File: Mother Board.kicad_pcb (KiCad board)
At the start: 2 copper layers, 127 x 124.5 mm, 102 parts, among them J1 Conn_01x02, J2 USB_B_Mini, J3 Conn_02x05_Odd_Even, J5 Conn_01x03, J6 Conn_01x03, SW1 SW_Push, U1 LM2595SX-3.3_NOPB, U2 LM2595SX-5.0_NOPB, U3 FT232RL, U4 STM32F407IGTx, U5 TPS2111APWR, Y1 Crystal_GND24

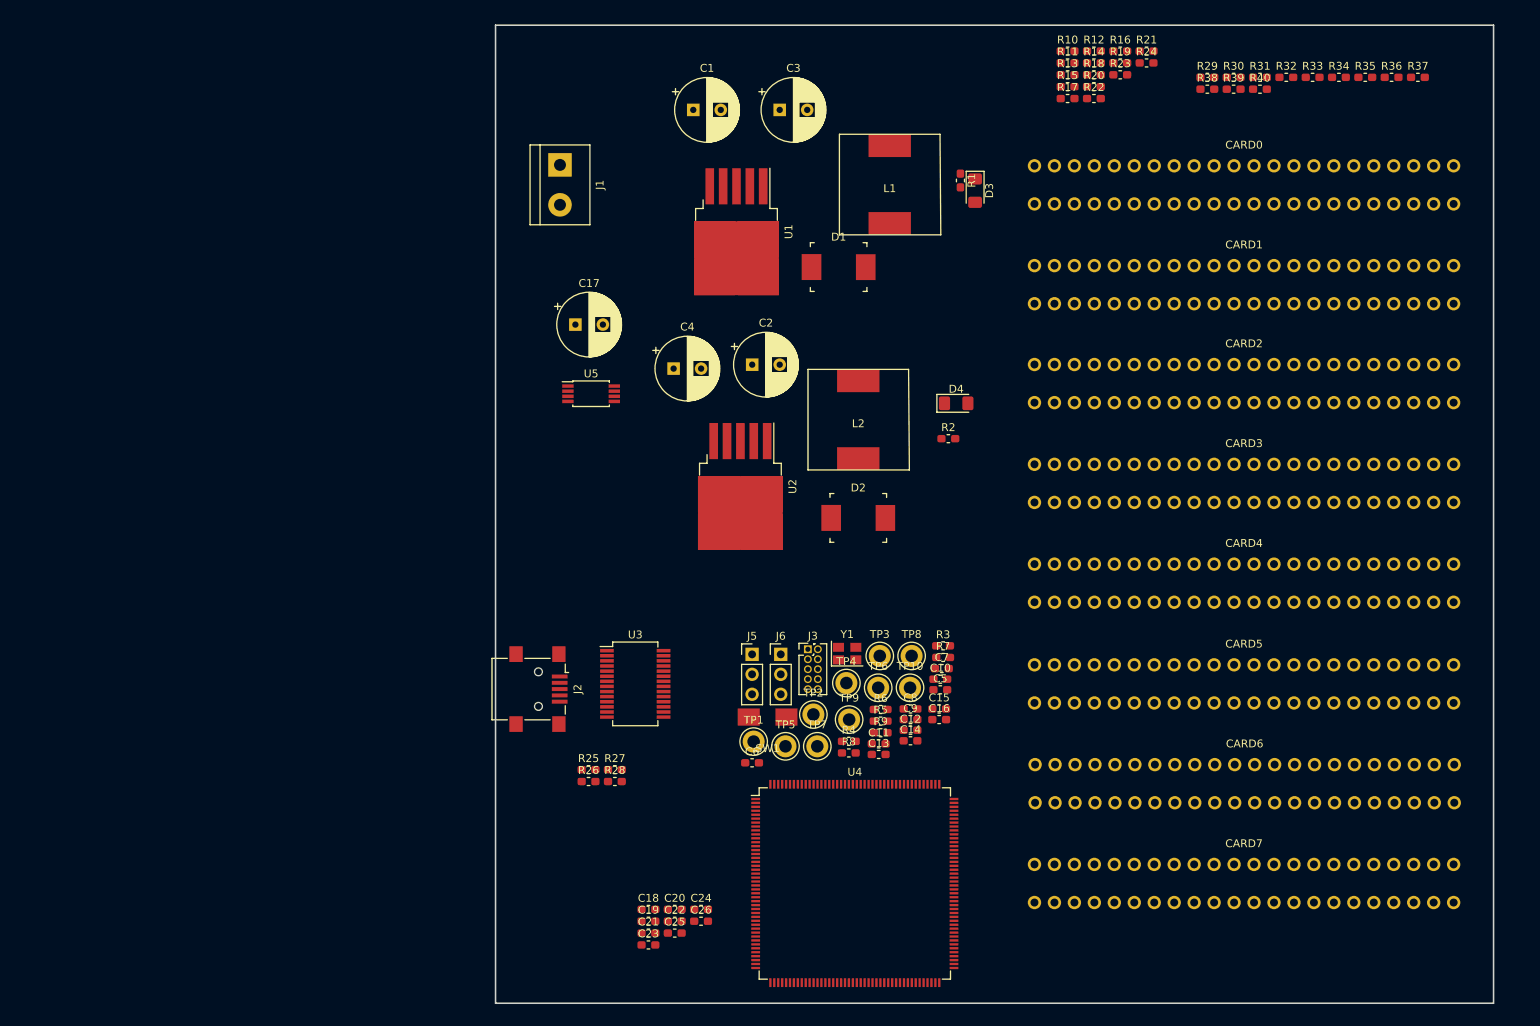
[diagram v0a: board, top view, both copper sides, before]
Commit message: Finished labeling card pins, changed rough layout
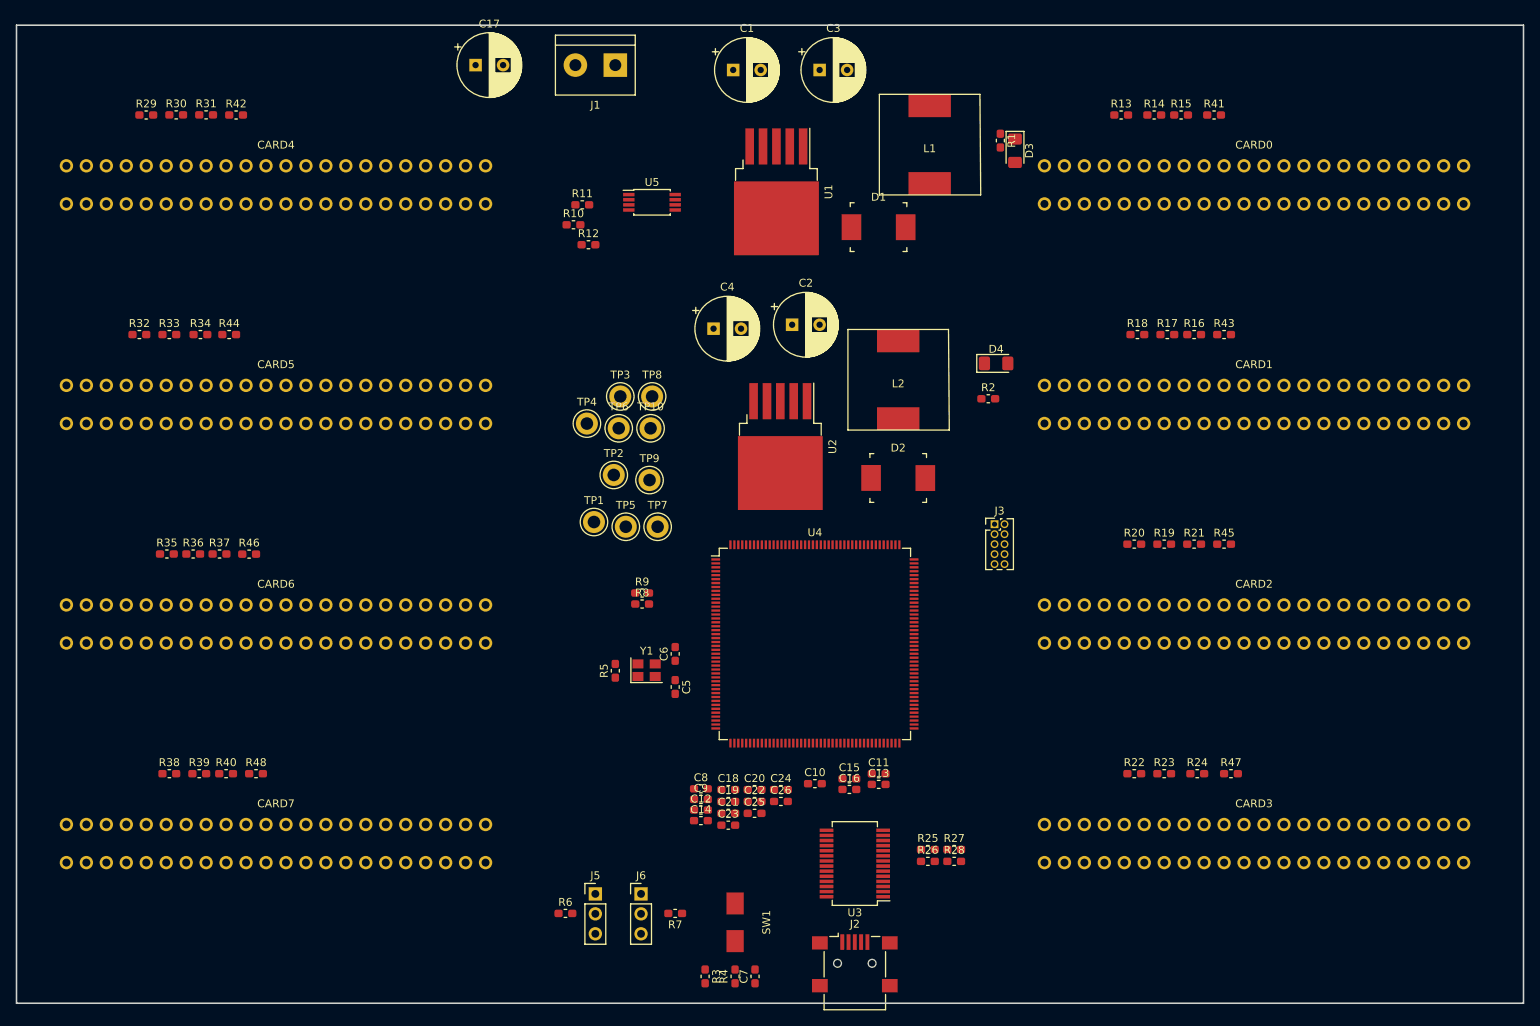
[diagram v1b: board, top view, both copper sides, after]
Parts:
- added R41: 10k, Resistor_SMD:R_0603_1608Metric_Pad1.05x0.95mm_HandSolder, F.Cu at (218.4, 47.0)
- added R42: 10k, Resistor_SMD:R_0603_1608Metric_Pad1.05x0.95mm_HandSolder, F.Cu at (94.0, 47.0)
- added R43: 10k, Resistor_SMD:R_0603_1608Metric_Pad1.05x0.95mm_HandSolder, F.Cu at (219.7, 74.9)
- added R44: 10k, Resistor_SMD:R_0603_1608Metric_Pad1.05x0.95mm_HandSolder, F.Cu at (93.1, 74.9)
- added R45: 10k, Resistor_SMD:R_0603_1608Metric_Pad1.05x0.95mm_HandSolder, F.Cu at (219.7, 101.6)
- added R46: 10k, Resistor_SMD:R_0603_1608Metric_Pad1.05x0.95mm_HandSolder, F.Cu at (95.6, 102.9)
- added R47: 10k, Resistor_SMD:R_0603_1608Metric_Pad1.05x0.95mm_HandSolder, F.Cu at (220.6, 130.8)
- added R48: 10k, Resistor_SMD:R_0603_1608Metric_Pad1.05x0.95mm_HandSolder, F.Cu at (96.5, 130.8)
- CARD0, CARD1, CARD2, CARD3, CARD4, CARD5, CARD6, CARD7: value Conn_02x22_Odd_Even -> Conn_02x22_Top_Bottom
- J1: footprint Connectors_Terminal_Blocks:TerminalBlock_bornier-2_P5.08mm -> TerminalBlock:TerminalBlock_bornier-2_P5.08mm
- U1, U2: footprint TO_SOT_Packages_SMD:TO-263-5_TabPin3 -> Package_TO_SOT_SMD:TO-263-5_TabPin3
- moved R35 164.1 mm to (85.2, 102.9)
- moved R36 164.1 mm to (88.5, 102.9)
- moved R37 164.1 mm to (91.9, 102.9)
- moved R38 158.2 mm to (85.5, 130.8)
- moved R39 157.8 mm to (89.3, 130.8)
- moved R40 157.8 mm to (92.7, 130.8)
- moved R32 149.6 mm to (81.7, 74.9)
- moved R33 149.1 mm to (85.5, 74.9)
- moved R34 148.5 mm to (89.4, 74.9)
- moved R29 135.1 mm to (82.5, 47.0)
- moved R30 134.6 mm to (86.4, 47.0)
- moved R31 134.2 mm to (90.2, 47.0)
- moved CARD4 133.2 mm to (99.1, 55.9)
- moved CARD5 128.2 mm to (99.1, 83.8)
- moved CARD6 124.9 mm to (99.1, 111.8)
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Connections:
- net CARD2_GPIO2 renamed CARD2_TIM1_CH3N
- net CARD2_GPIO4 renamed CARD2_GPIO0
- net CARD2_GPIO5 renamed CARD2_TIM10_CH1
- net CARD3_GPIO5 renamed CARD3_TIM11_CH1
- net Net-(CARD3-Pad35) renamed CARD3_TIM1_CH4
- net Net-(CARD3-Pad37) renamed CARD3_TIM3_CH4
- net Net-(CARD4-Pad35) renamed CARD4_TIM8_CH1
- net Net-(CARD4-Pad37) renamed CARD4_TIM5_CH1
- net Net-(CARD5-Pad37) renamed CARD5_TIM5_CH2
- net Net-(CARD6-Pad37) renamed CARD6_TIM5_CH3
- net Net-(CARD7-Pad37) renamed CARD7_TIM5_CH4
- CARD0 pad 10: +3V3 -> IC1_SDA
- CARD0 pad 11: +3V3 -> /CARD0_ADD0
- CARD0 pad 12: +3V3 -> /CARD0_ADD1
- CARD0 pad 13: GND -> /CARD0_ADD2
- CARD0 pad 14: GND -> CARD0_ENABLE
- CARD0 pad 15: GND -> CARD0_STATUS
- CARD0 pad 16: GND -> USART1_TX
- CARD0 pad 17: IC1_SCL -> USART1_RX
- CARD0 pad 18: SPI2_SCK_PI1 -> USART1_CTS
- CARD0 pad 19: IC1_SDA -> USART1_RTS
- CARD0 pad 20: SPI2_MISO_PI2 -> /CARD0_SENSE_POS
- CARD0 pad 21: /CARD0_ADD0 -> GND
- CARD0 pad 22: SPI2_MOSI_PI3 -> GND
- CARD0 pad 23: /CARD0_ADD1 -> +24V
- CARD0 pad 24: CARD0_CS -> +24V
- CARD0 pad 25: /CARD0_ADD2 -> +5V
- CARD0 pad 26: CARD0_TIM1_CH1 -> +5V
- CARD0 pad 27: CARD0_ENABLE -> +3V3
- CARD0 pad 28: CARD0_TIM1_CH2 -> +3V3
- CARD0 pad 29: CARD0_STATUS -> GND
- CARD0 pad 3: +24V -> +5V
- CARD0 pad 30: CARD0_TIM1_CH3 -> GND
- CARD0 pad 31: USART1_TX_PB6 -> SPI2_SCK
- CARD0 pad 32: CARD0_TIM1_CH4 -> SPI2_MISO
- CARD0 pad 33: USART1_RX_PB7 -> SPI2_MOSI
- CARD0 pad 34: CARD0_GPIO1 -> CARD0_CS
- CARD0 pad 35: USART1_CTS_PA11 -> CARD0_TIM1_CH1
- CARD0 pad 36: CARD0_GPIO2 -> CARD0_TIM1_CH1N
- CARD0 pad 37: USART1_RTS_PA12 -> CARD0_TIM3_CH1
- CARD0 pad 39: CARD0_GPIO5 -> CARD0_TIM9_CH1
- CARD0 pad 4: +24V -> +5V
- CARD0 pad 40: CARD0_GPIO4 -> CARD0_GPIO0
- CARD0 pad 41: GND -> CARD0_GPIO1
- CARD0 pad 42: GND -> CARD0_SENSE_NEG
- CARD0 pad 5: +5V -> +3V3
- CARD0 pad 6: +5V -> +3V3
- CARD0 pad 7: +5V -> GND
- CARD0 pad 8: +5V -> GND
- CARD0 pad 9: +3V3 -> IC1_SCL
- CARD1 pad 10: +3V3 -> IC1_SDA
- CARD1 pad 11: +3V3 -> /CARD1_ADD0
- CARD1 pad 12: +3V3 -> /CARD1_ADD1
- CARD1 pad 13: GND -> /CARD1_ADD2
- CARD1 pad 14: GND -> CARD1_ENABLE
- CARD1 pad 15: GND -> CARD1_STATUS
- CARD1 pad 16: GND -> USART6_TX
- CARD1 pad 17: IC1_SCL -> USART6_RX
- CARD1 pad 18: SPI2_SCK_PI1 -> USART6_CTS
- CARD1 pad 19: IC1_SDA -> USART6_RTS
- CARD1 pad 20: SPI2_MISO_PI2 -> /CARD1_SENSE_POS
- CARD1 pad 21: /CARD1_ADD0 -> GND
- CARD1 pad 22: SPI2_MOSI_PI3 -> GND
- CARD1 pad 23: /CARD1_ADD1 -> +24V
- CARD1 pad 24: CARD1_CS -> +24V
- CARD1 pad 25: /CARD1_ADD2 -> +5V
- CARD1 pad 26: CARD1_TIM8_CH1 -> +5V
- CARD1 pad 27: CARD1_ENABLE -> +3V3
- CARD1 pad 28: CARD1_TIM8_CH2 -> +3V3
- CARD1 pad 29: CARD1_STATUS -> GND
- CARD1 pad 3: +24V -> +5V
- CARD1 pad 30: CARD1_TIM8_CH3 -> GND
- CARD1 pad 31: USART3_TX_PB10 -> SPI2_SCK_PI1
- CARD1 pad 32: CARD1_TIM8_CH4 -> SPI2_MISO_PI2
- CARD1 pad 33: USART3_RX_PB11 -> SPI2_MOSI_PI3
- CARD1 pad 34: CARD1_GPIO1 -> CARD1_CS
- CARD1 pad 35: USART3_CTS_PB13 -> CARD1_TIM1_CH2
- CARD1 pad 36: CARD1_GPIO2 -> CARD1_TIM1_CH2N
- CARD1 pad 37: USART3_RTS_PB14 -> CARD1_TIM3_CH2
- CARD1 pad 39: CARD1_GPIO5 -> CARD1_TIM9_CH2
- CARD1 pad 4: +24V -> +5V
- CARD1 pad 40: CARD1_GPIO4 -> CARD1_GPIO0
- CARD1 pad 41: GND -> CARD1_GPIO1
- CARD1 pad 42: GND -> CARD1_SENSE_NEG
- CARD1 pad 5: +5V -> +3V3
- CARD1 pad 6: +5V -> +3V3
- CARD1 pad 7: +5V -> GND
- CARD1 pad 8: +5V -> GND
- CARD1 pad 9: +3V3 -> IC1_SCL
- CARD2 pad 10: +3V3 -> IC1_SDA
- CARD2 pad 11: +3V3 -> /CARD2_ADD0
- CARD2 pad 12: +3V3 -> /CARD2_ADD1
- CARD2 pad 13: GND -> /CARD2_ADD2
- CARD2 pad 14: GND -> CARD2_ENABLE
- CARD2 pad 15: GND -> CARD2_STATUS
- CARD2 pad 16: GND -> USART3_TX
- CARD2 pad 17: IC1_SCL -> USART3_RX
- CARD2 pad 18: SPI2_SCK_PI1 -> USART3_CTS
- CARD2 pad 19: IC1_SDA -> USART3_RTS
- CARD2 pad 20: SPI2_MISO_PI2 -> /CARD2_SENSE_POS
- CARD2 pad 21: /CARD2_ADD0 -> GND
- CARD2 pad 22: SPI2_MOSI_PI3 -> GND
- CARD2 pad 23: /CARD2_ADD1 -> +24V
- CARD2 pad 24: CARD2_CS -> +24V
- CARD2 pad 25: /CARD2_ADD2 -> +5V
- CARD2 pad 26: CARD2_TIM8_CH1 -> +5V
- CARD2 pad 27: CARD2_ENABLE -> +3V3
- CARD2 pad 28: CARD2_TIM8_CH2 -> +3V3
- CARD2 pad 29: CARD2_STATUS -> GND
- CARD2 pad 3: +24V -> +5V
- CARD2 pad 30: CARD2_TIM8_CH3 -> GND
- CARD2 pad 31: USART3_TX_PD8 -> SPI2_SCK_PI1
- CARD2 pad 32: CARD2_TIM8_CH4 -> SPI2_MISO_PI2
- CARD2 pad 33: USART3_RX_PD9 -> SPI2_MOSI_PI3
- CARD2 pad 34: CARD2_GPIO1 -> CARD2_CS
- CARD2 pad 35: USART3_CTS_PD11 -> CARD2_TIM1_CH3
- CARD2 pad 37: USART3_RTS_PD12 -> CARD2_TIM3_CH3
- CARD2 pad 4: +24V -> +5V
- CARD2 pad 41: GND -> CARD2_GPIO1
- CARD2 pad 42: GND -> CARD2_SENSE_NEG
- CARD2 pad 5: +5V -> +3V3
- CARD2 pad 6: +5V -> +3V3
- CARD2 pad 7: +5V -> GND
- CARD2 pad 8: +5V -> GND
- CARD2 pad 9: +3V3 -> IC1_SCL
- CARD3 pad 10: +3V3 -> IC1_SDA
- CARD3 pad 11: +3V3 -> /CARD3_ADD0
- CARD3 pad 12: +3V3 -> /CARD3_ADD1
- CARD3 pad 13: GND -> /CARD3_ADD2
- CARD3 pad 14: GND -> CARD3_ENABLE
- CARD3 pad 15: GND -> CARD3_STATUS
- CARD3 pad 16: GND -> UART4_TX
- CARD3 pad 17: IC1_SCL -> UART4_RX
- CARD3 pad 18: SPI2_SCK_PI1 -> CARD3_GPIO3
- CARD3 pad 19: IC1_SDA -> CARD3_GPIO2
- CARD3 pad 20: SPI2_MISO_PI2 -> /CARD3_SENSE_POS
- CARD3 pad 21: /CARD3_ADD0 -> GND
- CARD3 pad 22: SPI2_MOSI_PI3 -> GND
- CARD3 pad 23: /CARD3_ADD1 -> +24V
- CARD3 pad 24: CARD3_CS -> +24V
- CARD3 pad 25: /CARD3_ADD2 -> +5V
- CARD3 pad 26: CARD3_TIM8_CH1 -> +5V
- CARD3 pad 27: CARD3_ENABLE -> +3V3
- CARD3 pad 28: CARD3_TIM8_CH2 -> +3V3
- CARD3 pad 29: CARD3_STATUS -> GND
- CARD3 pad 3: +24V -> +5V
- CARD3 pad 30: CARD3_TIM8_CH3 -> GND
- CARD3 pad 31: UART5_TX_PC12 -> SPI2_SCK_PI1
- CARD3 pad 32: CARD3_TIM8_CH4 -> SPI2_MISO_PI2
- CARD3 pad 33: UART5_RX_PD2 -> SPI2_MOSI_PI3
- CARD3 pad 34: CARD3_GPIO1 -> CARD3_CS
- CARD3 pad 36: CARD3_GPIO2 -> CARD3_GPIO4
- CARD3 pad 38: Net-(CARD3-Pad38) -> CARD3_TIM2_CH4
- CARD3 pad 4: +24V -> +5V
- CARD3 pad 40: CARD3_GPIO4 -> CARD3_GPIO0
- CARD3 pad 41: GND -> CARD3_GPIO1
- CARD3 pad 42: GND -> CARD3_SENSE_NEG
- CARD3 pad 5: +5V -> +3V3
- CARD3 pad 6: +5V -> +3V3
- CARD3 pad 7: +5V -> GND
- CARD3 pad 8: +5V -> GND
- CARD3 pad 9: +3V3 -> IC1_SCL
- CARD4 pad 10: +3V3 -> IC1_SDA
- CARD4 pad 11: +3V3 -> /CARD4_ADD0
- CARD4 pad 12: +3V3 -> /CARD4_ADD1
- CARD4 pad 13: GND -> /CARD4_ADD2
- CARD4 pad 14: GND -> CARD4_ENABLE
- CARD4 pad 15: GND -> CARD4_STATUS
- CARD4 pad 16: GND -> CARD4_GPIO5
- CARD4 pad 17: IC1_SCL -> CARD4_GPIO4
- CARD4 pad 18: SPI2_SCK_PI1 -> CARD4_GPIO3
- CARD4 pad 19: IC1_SDA -> CARD4_GPIO2
- CARD4 pad 20: SPI2_MISO_PI2 -> /CARD4_SENSE_POS
- CARD4 pad 21: /CARD4_ADD0 -> GND
- CARD4 pad 22: SPI2_MOSI_PI3 -> GND
- CARD4 pad 23: /CARD4_ADD1 -> +24V
- CARD4 pad 24: CARD4_CS -> +24V
- CARD4 pad 25: /CARD4_ADD2 -> +5V
- CARD4 pad 26: CARD4_TIM1_CH1 -> +5V
- CARD4 pad 27: CARD4_ENABLE -> +3V3
- CARD4 pad 28: CARD4_TIM1_CH2 -> +3V3
- CARD4 pad 29: CARD4_STATUS -> GND
- CARD4 pad 3: +24V -> +5V
- CARD4 pad 30: CARD4_TIM1_CH3 -> GND
- CARD4 pad 31: Net-(CARD4-Pad31) -> SPI2_SCK_PI1
- CARD4 pad 32: CARD4_TIM1_CH4 -> SPI2_MISO_PI2
- CARD4 pad 33: Net-(CARD4-Pad33) -> SPI2_MOSI_PI3
- CARD4 pad 34: CARD4_GPIO1 -> CARD4_CS
- CARD4 pad 36: CARD4_GPIO2 -> CARD4_TIM8_CH1N
- CARD4 pad 38: CARD4_TIM3_CH1 -> CARD4_TIM4_CH1
- CARD4 pad 39: CARD4_GPIO5 -> CARD4_TIM12_CH1
- CARD4 pad 4: +24V -> +5V
- CARD4 pad 40: CARD4_GPIO4 -> CARD4_GPIO0
- CARD4 pad 41: GND -> CARD4_GPIO1
- CARD4 pad 42: GND -> CARD4_SENSE_NEG
- CARD4 pad 5: +5V -> +3V3
- CARD4 pad 6: +5V -> +3V3
- CARD4 pad 7: +5V -> GND
- CARD4 pad 8: +5V -> GND
- CARD4 pad 9: +3V3 -> IC1_SCL
- CARD5 pad 10: +3V3 -> IC1_SDA
- CARD5 pad 11: +3V3 -> /CARD5_ADD0
- CARD5 pad 12: +3V3 -> /CARD5_ADD1
- CARD5 pad 13: GND -> /CARD5_ADD2
- CARD5 pad 14: GND -> CARD5_ENABLE
- CARD5 pad 15: GND -> CARD5_STATUS
- CARD5 pad 16: GND -> CARD5_GPIO5
- CARD5 pad 17: IC1_SCL -> CARD5_GPIO4
- CARD5 pad 18: SPI2_SCK_PI1 -> CARD5_GPIO3
- CARD5 pad 19: IC1_SDA -> CARD5_GPIO2
- CARD5 pad 20: SPI2_MISO_PI2 -> /CARD5_SENSE_POS
- CARD5 pad 21: /CARD5_ADD0 -> GND
- CARD5 pad 22: SPI2_MOSI_PI3 -> GND
- CARD5 pad 23: /CARD5_ADD1 -> +24V
- CARD5 pad 24: CARD5_CS -> +24V
- CARD5 pad 25: /CARD5_ADD2 -> +5V
- CARD5 pad 26: CARD5_TIM8_CH1 -> +5V
- CARD5 pad 27: CARD5_ENABLE -> +3V3
- CARD5 pad 28: CARD5_TIM8_CH2 -> +3V3
- CARD5 pad 29: CARD5_STATUS -> GND
- CARD5 pad 3: +24V -> +5V
- CARD5 pad 30: CARD5_TIM8_CH3 -> GND
- CARD5 pad 31: Net-(CARD5-Pad31) -> SPI2_SCK_PI1
- CARD5 pad 32: CARD5_TIM8_CH4 -> SPI2_MISO_PI2
- CARD5 pad 33: Net-(CARD5-Pad33) -> SPI2_MOSI_PI3
- CARD5 pad 34: CARD5_GPIO1 -> CARD5_CS
- CARD5 pad 35: Net-(CARD5-Pad35) -> CARD5_TIM8_CH2
- CARD5 pad 36: CARD5_GPIO2 -> CARD5_TIM8_CH2N
- CARD5 pad 38: CARD5_TIM3_CH2 -> CARD5_TIM4_CH2
- CARD5 pad 39: CARD5_GPIO5 -> CARD5_TIM12_CH2
- CARD5 pad 4: +24V -> +5V
- CARD5 pad 40: CARD5_GPIO4 -> CARD5_GPIO0
- CARD5 pad 41: GND -> CARD5_GPIO1
- CARD5 pad 42: GND -> CARD5_SENSE_NEG
- CARD5 pad 5: +5V -> +3V3
- CARD5 pad 6: +5V -> +3V3
- CARD5 pad 7: +5V -> GND
- CARD5 pad 8: +5V -> GND
- CARD5 pad 9: +3V3 -> IC1_SCL
- CARD6 pad 10: +3V3 -> IC1_SDA
- CARD6 pad 11: +3V3 -> /CARD6_ADD0
- CARD6 pad 12: +3V3 -> /CARD6_ADD1
- CARD6 pad 13: GND -> /CARD6_ADD2
- CARD6 pad 14: GND -> CARD6_ENABLE
- CARD6 pad 15: GND -> CARD6_STATUS
- CARD6 pad 16: GND -> CARD6_GPIO5
- CARD6 pad 17: IC1_SCL -> CARD6_GPIO4
- CARD6 pad 18: SPI2_SCK_PI1 -> CARD6_GPIO3
- CARD6 pad 19: IC1_SDA -> CARD6_GPIO2
- CARD6 pad 20: SPI2_MISO_PI2 -> /CARD6_SENSE_POS
- CARD6 pad 21: /CARD6_ADD0 -> GND
- CARD6 pad 22: SPI2_MOSI_PI3 -> GND
- CARD6 pad 23: /CARD6_ADD1 -> +24V
- CARD6 pad 24: CARD6_CS -> +24V
- CARD6 pad 25: /CARD6_ADD2 -> +5V
- CARD6 pad 26: CARD6_TIM8_CH1 -> +5V
- CARD6 pad 27: CARD6_ENABLE -> +3V3
- CARD6 pad 28: CARD6_TIM8_CH2 -> +3V3
- CARD6 pad 29: CARD6_STATUS -> GND
- CARD6 pad 3: +24V -> +5V
- CARD6 pad 30: CARD6_TIM8_CH3 -> GND
- CARD6 pad 31: Net-(CARD6-Pad31) -> SPI2_SCK_PI1
- CARD6 pad 32: CARD6_TIM8_CH4 -> SPI2_MISO_PI2
- CARD6 pad 33: Net-(CARD6-Pad33) -> SPI2_MOSI_PI3
- CARD6 pad 34: CARD6_GPIO1 -> CARD6_CS
- CARD6 pad 35: Net-(CARD6-Pad35) -> CARD6_TIM8_CH3
- CARD6 pad 36: CARD6_GPIO2 -> CARD6_TIM8_CH3N
- CARD6 pad 38: CARD6_TIM3_CH3 -> CARD6_TIM4_CH3
- CARD6 pad 39: CARD6_GPIO5 -> CARD6_TIM13_CH1
- CARD6 pad 4: +24V -> +5V
- CARD6 pad 40: CARD6_GPIO4 -> CARD6_GPIO0
- CARD6 pad 41: GND -> CARD6_GPIO1
- CARD6 pad 42: GND -> CARD6_SENSE_NEG
- CARD6 pad 5: +5V -> +3V3
- CARD6 pad 6: +5V -> +3V3
- CARD6 pad 7: +5V -> GND
- CARD6 pad 8: +5V -> GND
- CARD6 pad 9: +3V3 -> IC1_SCL
- CARD7 pad 10: +3V3 -> IC1_SDA
- CARD7 pad 11: +3V3 -> /CARD7_ADD0
- CARD7 pad 12: +3V3 -> /CARD7_ADD1
- CARD7 pad 13: GND -> /CARD7_ADD2
- CARD7 pad 14: GND -> CARD7_ENABLE
- CARD7 pad 15: GND -> CARD7_STATUS
- CARD7 pad 16: GND -> CARD7_GPIO5
- CARD7 pad 17: IC1_SCL -> CARD7_GPIO4
- CARD7 pad 18: SPI2_SCK_PI1 -> CARD7_GPIO3
- CARD7 pad 19: IC1_SDA -> CARD7_GPIO2
- CARD7 pad 20: SPI2_MISO_PI2 -> /CARD7_SENSE_POS
- CARD7 pad 21: /CARD7_ADD0 -> GND
- CARD7 pad 22: SPI2_MOSI_PI3 -> GND
- CARD7 pad 23: /CARD7_ADD1 -> +24V
- CARD7 pad 24: CARD7_CS -> +24V
- CARD7 pad 25: /CARD7_ADD2 -> +5V
- CARD7 pad 26: CARD7_TIM8_CH1 -> +5V
- CARD7 pad 27: CARD7_ENABLE -> +3V3
- CARD7 pad 28: CARD7_TIM8_CH2 -> +3V3
- CARD7 pad 29: CARD7_STATUS -> GND
- CARD7 pad 3: +24V -> +5V
- CARD7 pad 30: CARD7_TIM8_CH3 -> GND
- CARD7 pad 31: Net-(CARD7-Pad31) -> SPI2_SCK_PI1
- CARD7 pad 32: CARD7_TIM8_CH4 -> SPI2_MISO_PI2
- CARD7 pad 33: Net-(CARD7-Pad33) -> SPI2_MOSI_PI3
- CARD7 pad 34: CARD7_GPIO1 -> CARD7_CS
- CARD7 pad 35: Net-(CARD7-Pad35) -> CARD7_TIM8_CH4
- CARD7 pad 36: CARD7_GPIO2 -> CARD7_GPIO6
- CARD7 pad 38: CARD7_TIM3_CH4 -> CARD7_TIM4_CH4
- CARD7 pad 39: CARD7_GPIO5 -> CARD7_TIM14_CH1
- CARD7 pad 4: +24V -> +5V
- CARD7 pad 40: CARD7_GPIO4 -> CARD7_GPIO0
- CARD7 pad 41: GND -> CARD7_GPIO1
- CARD7 pad 42: GND -> CARD7_SENSE_NEG
- CARD7 pad 5: +5V -> +3V3
- CARD7 pad 6: +5V -> +3V3
- CARD7 pad 7: +5V -> GND
- CARD7 pad 8: +5V -> GND
- CARD7 pad 9: +3V3 -> IC1_SCL
- U4 pad 100: USART3_RTS_PD12 -> Net-(U4-Pad100)
- U4 pad 122: USART1_CTS_PA11 -> Net-(U4-Pad122)
- U4 pad 123: USART1_RTS_PA12 -> Net-(U4-Pad123)
- U4 pad 128: CARD1_GPIO1 -> Net-(U4-Pad128)
- U4 pad 129: CARD1_GPIO2 -> Net-(U4-Pad129)
- U4 pad 133: CARD1_TIM8_CH4 -> Net-(U4-Pad133)
- U4 pad 134: CARD1_GPIO4 -> Net-(U4-Pad134)
- U4 pad 141: UART5_TX_PC12 -> Net-(U4-Pad141)
- U4 pad 144: UART5_RX_PD2 -> Net-(U4-Pad144)
- U4 pad 145: USART2_CTS_PD3 -> Net-(U4-Pad145)
- U4 pad 146: USART2_RTS_PD4 -> Net-(U4-Pad146)
- U4 pad 147: USART2_TX_PD5 -> Net-(U4-Pad147)
- U4 pad 150: USART2_RX_PD6 -> Net-(U4-Pad150)
- U4 pad 164: USART1_TX_PB6 -> Net-(U4-Pad164)
- U4 pad 165: USART1_RX_PB7 -> Net-(U4-Pad165)
- U4 pad 173: CARD1_GPIO5 -> Net-(U4-Pad173)
- U4 pad 174: CARD1_TIM8_CH1 -> Net-(U4-Pad174)
- U4 pad 175: CARD1_TIM8_CH2 -> Net-(U4-Pad175)
- U4 pad 176: CARD1_TIM8_CH3 -> Net-(U4-Pad176)
- U4 pad 41: CARD1_TIM2_CH2 -> Net-(U4-Pad41)
- U4 pad 42: CARD2_TIM2_CH3 -> Net-(U4-Pad42)
- U4 pad 47: CARD3_TIM2_CH4 -> Net-(U4-Pad47)
- U4 pad 51: CARD0_TIM2_CH1 -> Net-(U4-Pad51)
- U4 pad 52: CARD4_TIM3_CH1 -> Net-(U4-Pad52)
- U4 pad 53: CARD5_TIM3_CH2 -> Net-(U4-Pad53)
- U4 pad 56: CARD6_TIM3_CH3 -> Net-(U4-Pad56)
- U4 pad 57: CARD7_TIM3_CH4 -> Net-(U4-Pad57)
- U4 pad 68: CARD0_GPIO4 -> Net-(U4-Pad68)
- U4 pad 69: CARD0_GPIO1 -> Net-(U4-Pad69)
- U4 pad 70: CARD0_TIM1_CH1 -> Net-(U4-Pad70)
- U4 pad 73: CARD0_GPIO2 -> Net-(U4-Pad73)
- U4 pad 74: CARD0_TIM1_CH2 -> Net-(U4-Pad74)
- U4 pad 76: CARD0_TIM1_CH3 -> Net-(U4-Pad76)
- U4 pad 77: CARD0_TIM1_CH4 -> Net-(U4-Pad77)
- U4 pad 78: CARD0_GPIO5 -> Net-(U4-Pad78)
- U4 pad 79: USART3_TX_PB10 -> Net-(U4-Pad79)
- U4 pad 80: USART3_RX_PB11 -> Net-(U4-Pad80)
- U4 pad 93: USART3_CTS_PB13 -> Net-(U4-Pad93)
- U4 pad 94: USART3_RTS_PB14 -> Net-(U4-Pad94)
- U4 pad 96: USART3_TX_PD8 -> Net-(U4-Pad96)
- U4 pad 97: USART3_RX_PD9 -> Net-(U4-Pad97)
- U4 pad 99: USART3_CTS_PD11 -> Net-(U4-Pad99)
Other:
- board size 127 x 124.5 mm -> 191.8 x 124.5 mm

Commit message: Moved power supply to external board.  Reworked rough layout
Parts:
- removed D1, D2: D_Schottky, digikey-footprints:DO-214AB
- removed L1, L2: L, my_inductors:Wurth_SMD_Inductor_7447709101
- removed R10: 10K, Resistor_SMD:R_0603_1608Metric_Pad1.05x0.95mm_HandSolder
- removed R11: 265R, Resistor_SMD:R_0603_1608Metric_Pad1.05x0.95mm_HandSolder
- removed R12: 400R, Resistor_SMD:R_0603_1608Metric_Pad1.05x0.95mm_HandSolder
- removed U1: LM2595SX-3.3_NOPB, Package_TO_SOT_SMD:TO-263-5_TabPin3
- removed U2: LM2595SX-5.0_NOPB, Package_TO_SOT_SMD:TO-263-5_TabPin3
- added J4: Conn_01x04, TerminalBlock:TerminalBlock_bornier-4_P5.08mm, F.Cu at (88.9, 96.5)
- added J7: Conn_01x04, TerminalBlock:TerminalBlock_bornier-4_P5.08mm, F.Cu at (88.9, 119.4)
- added REF**: MountingHole_4.5mm, MountingHole:MountingHole_4.5mm, F.Cu at (314.3, 71.8)
- added REF**: MountingHole_4.5mm, MountingHole:MountingHole_4.5mm, F.Cu at (258.4, 151.8)
- added REF**: MountingHole_4.5mm, MountingHole:MountingHole_4.5mm, F.Cu at (230.5, 151.8)
- added REF**: MountingHole_4.5mm, MountingHole:MountingHole_4.5mm, F.Cu at (202.6, 151.8)
- added REF**: MountingHole_4.5mm, MountingHole:MountingHole_4.5mm, F.Cu at (174.6, 151.8)
- added REF**: MountingHole_4.5mm, MountingHole:MountingHole_4.5mm, F.Cu at (146.7, 151.8)
- added REF**: MountingHole_4.5mm, MountingHole:MountingHole_4.5mm, F.Cu at (118.7, 71.8)
- added REF**: MountingHole_4.5mm, MountingHole:MountingHole_4.5mm, F.Cu at (118.7, 151.8)
- added REF**: MountingHole_4.5mm, MountingHole:MountingHole_4.5mm, F.Cu at (286.4, 71.8)
- added REF**: MountingHole_4.5mm, MountingHole:MountingHole_4.5mm, F.Cu at (258.4, 71.8)
- added REF**: MountingHole_4.5mm, MountingHole:MountingHole_4.5mm, F.Cu at (230.5, 71.8)
- added REF**: MountingHole_4.5mm, MountingHole:MountingHole_4.5mm, F.Cu at (202.6, 71.8)
- added REF**: MountingHole_4.5mm, MountingHole:MountingHole_4.5mm, F.Cu at (174.6, 71.8)
- added REF**: MountingHole_4.5mm, MountingHole:MountingHole_4.5mm, F.Cu at (146.7, 71.8)
- added REF**: MountingHole_4.5mm, MountingHole:MountingHole_4.5mm, F.Cu at (314.3, 151.8)
- added REF**: MountingHole_4.5mm, MountingHole:MountingHole_4.5mm, F.Cu at (286.4, 151.8)
- J1: value Conn_01x02 -> Conn_01x04; footprint TerminalBlock:TerminalBlock_bornier-2_P5.08mm -> TerminalBlock:TerminalBlock_bornier-4_P5.08mm
- moved TP10 174.5 mm to (297.2, 175.1)
- moved TP2 174.5 mm to (292.5, 181.1)
- moved TP3 174.5 mm to (293.4, 171.1)
- moved TP4 174.5 mm to (289.1, 174.5)
- moved TP5 174.5 mm to (294.1, 187.7)
- moved TP6 174.5 mm to (293.2, 175.1)
- moved TP7 174.5 mm to (298.1, 187.7)
- moved TP8 174.5 mm to (297.4, 171.1)
- moved TP1 174.5 mm to (290.0, 187.1)
- moved TP9 174.5 mm to (297.1, 181.7)
- moved D3 151.0 mm to (117.5, 182.2), turned to 180 degrees
- moved R1 148.3 mm to (118.0, 179.2), turned to 180 degrees
- moved C3 143.6 mm to (91.4, 162.6), turned to 270 degrees
- moved C1 142.7 mm to (101.6, 172.7), turned to 270 degrees
- moved C17 136.1 mm to (91.4, 172.7), turned to 270 degrees
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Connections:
- C2 pad 1: +24V -> Net-(C2-Pad1)
- C2 pad 2: GND -> Net-(C2-Pad2)
- J1 pad 2: +24V -> GND
- U5 pad 1: GND -> Net-(U5-Pad1)
- U5 pad 3: GND -> Net-(U5-Pad3)
- U5 pad 7: Net-(C1-Pad1) -> Net-(U5-Pad7)
- U5 pad 8: Net-(C4-Pad1) -> Net-(U5-Pad8)
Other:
- board size 191.8 x 124.5 mm -> 236.2 x 139.7 mm

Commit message: last commit before shifting to prototype version
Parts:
- added REF**: MountingHole_4.5mm, MountingHole:MountingHole_4.5mm, F.Cu at (89.2, 71.8)
- moved C1 83.9 mm to (99.1, 88.9)
- moved C3 64.0 mm to (99.1, 99.1)
- moved C2 43.8 mm to (99.1, 109.2)
- moved C17 41.3 mm to (99.1, 132.1)
- moved C4 22.6 mm to (99.1, 121.0)
- moved J1 7.62 mm to (88.9, 81.3)
- moved J4 7.62 mm to (88.9, 104.1)
- moved J7 7.62 mm to (88.9, 127.0)
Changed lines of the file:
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@@
     (tracks 0)
     (zones 0)
-    (modules 119)
+    (modules 120)
     (nets 366)
   )
@@
   )
   (module MountingHole:MountingHole_4.5mm locked (layer F.Cu)
+    (at 89.22 71.76)
+    (descr "Mounting Hole 4.5mm, no annular")
+    (tags "mounting hole 4.5mm no annular")
+    (attr virtual)
+    (fp_text reference REF** (at 0 -5.5) (layer F.SilkS)
+      (effects (font (size 1 1) (thickness 0.15)))
+    )
+    (fp_text value MountingHole_4.5mm (at 0 5.5) (layer F.Fab)
+      (effects (font (size 1 1) (thickness 0.15)))
+    )
+    (fp_text user %R (at 0.3 0) (layer F.Fab)
+      (effects (font (size 1 1) (thickness 0.15)))
+    )
+    (fp_circle (center 0 0) (end 4.5 0) (layer Cmts.User) (width 0.15))
+    (fp_circle (center 0 0) (end 4.75 0) (layer F.CrtYd) (width 0.05))
+    (pad 1 np_thru_hole circle (at 0 0) (size 4.5 4.5) (drill 4.5) (layers *.Cu *.Mask))
+  )
+  (module MountingHole:MountingHole_4.5mm locked (layer F.Cu)
     (at 314.32 71.76)
     (descr "Mounting Hole 4.5mm, no annular")
@@
   )
   (module Capacitor_THT:CP_Radial_D8.0mm_P3.50mm (layer F.Cu)
-    (at 91.44 162.56 270)
+    (at 99.06 99.06 270)
     (descr "CP, Radial series, Radial, pin pitch=3.50mm, , diameter=8mm, Electrolytic Capacitor")
     (tags "CP Radial series Radial pin pitch 3.50mm  diameter 8mm Electrolytic Capacitor")
@@
   )
   (module Capacitor_THT:CP_Radial_D8.0mm_P3.50mm (layer F.Cu)
-    (at 91.44 142.24 270)
+    (at 99.06 120.96 270)
     (descr "CP, Radial series, Radial, pin pitch=3.50mm, , diameter=8mm, Electrolytic Capacitor")
     (tags "CP Radial series Radial pin pitch 3.50mm  diameter 8mm Electrolytic Capacitor")
@@
   )
   (module Capacitor_THT:CP_Radial_D8.0mm_P3.50mm (layer F.Cu)
-    (at 91.44 172.72 270)
+    (at 99.06 132.08 270)
     (descr "CP, Radial series, Radial, pin pitch=3.50mm, , diameter=8mm, Electrolytic Capacitor")
     (tags "CP Radial series Radial pin pitch 3.50mm  diameter 8mm Electrolytic Capacitor")
@@
   )
   (module Capacitor_THT:CP_Radial_D8.0mm_P3.50mm (layer F.Cu)
-    (at 101.6 172.72 270)
+    (at 99.06 88.9 270)
     (descr "CP, Radial series, Radial, pin pitch=3.50mm, , diameter=8mm, Electrolytic Capacitor")
     (tags "CP Radial series Radial pin pitch 3.50mm  diameter 8mm Electrolytic Capacitor")
@@
   )
   (module Capacitor_THT:CP_Radial_D8.0mm_P3.50mm (layer F.Cu)
-    (at 91.44 152.4 270)
+    (at 99.06 109.22 270)
     (descr "CP, Radial series, Radial, pin pitch=3.50mm, , diameter=8mm, Electrolytic Capacitor")
     (tags "CP Radial series Radial pin pitch 3.50mm  diameter 8mm Electrolytic Capacitor")
@@
   )
   (module TerminalBlock:TerminalBlock_bornier-4_P5.08mm (layer F.Cu)
-    (at 88.9 96.52 270)
+    (at 88.9 104.14 270)
     (descr "simple 4-pin terminal block, pitch 5.08mm, revamped version of bornier4")
     (tags "terminal block bornier4")
@@
   )
   (module TerminalBlock:TerminalBlock_bornier-4_P5.08mm (layer F.Cu)
-    (at 88.9 119.38 270)
+    (at 88.9 127 270)
     (descr "simple 4-pin terminal block, pitch 5.08mm, revamped version of bornier4")
     (tags "terminal block bornier4")
@@
   )
   (module TerminalBlock:TerminalBlock_bornier-4_P5.08mm (layer F.Cu)
-    (at 88.9 73.66 270)
+    (at 88.9 81.28 270)
     (descr "simple 4-pin terminal block, pitch 5.08mm, revamped version of bornier4")
     (tags "terminal block bornier4")
